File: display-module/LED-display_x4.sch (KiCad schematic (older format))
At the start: 8 parts, among them J1 Conn_DP1, J2 Conn_DP1, M1 Conn_01x01, M2 Conn_01x01, M3 Conn_01x01, M4 Conn_01x01

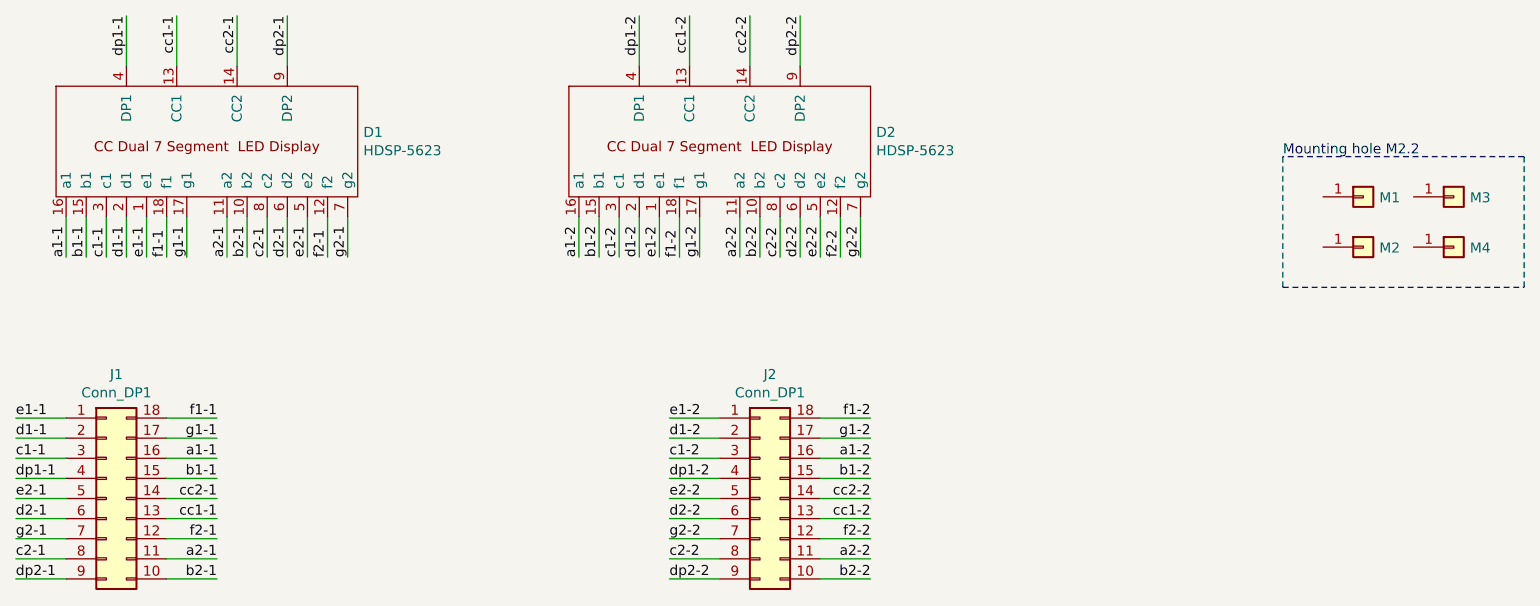
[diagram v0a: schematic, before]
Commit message: update file
I make mistake in schematics library & footprint library
now devices are correct, I divided 7 segment display at
two separate CA & CC

bye!
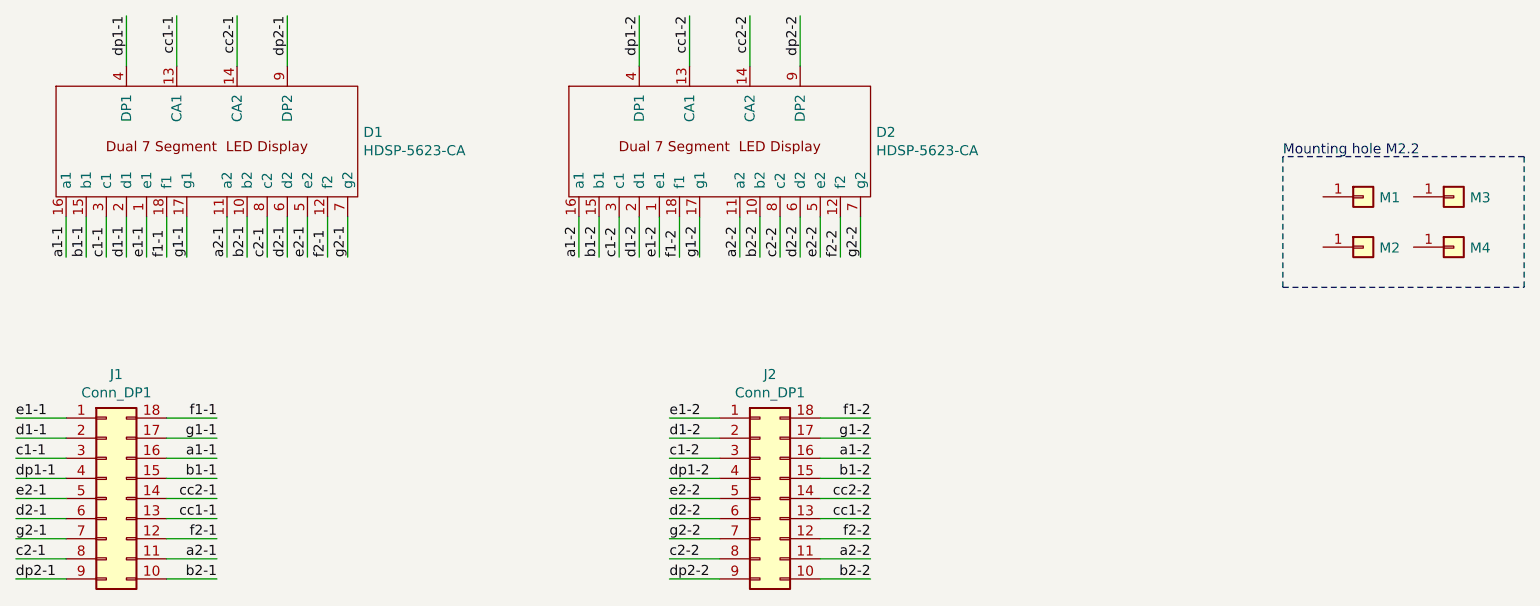
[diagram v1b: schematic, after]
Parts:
- removed D1, D2: HDSP-5623, led_display:package_led_display_0.56in_dual, symbol LED_Display:HDSP-5623
- added D1, D2: HDSP-5623-CA, led_display:package_led_display_0.56in_dual, symbol LED_Display:HDSP-5623-CA
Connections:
- net a1-1: now also D1.16 (a1)
- net a1-2: now also D2.16 (a1)
- net a2-1: now also D1.11 (a2)
- net a2-2: now also D2.11 (a2)
- net b1-1: now also D1.15 (b1)
- net b1-2: now also D2.15 (b1)
- net b2-1: now also D1.10 (b2)
- net b2-2: now also D2.10 (b2)
- net c1-1: now also D1.3 (c1)
- net c1-2: now also D2.3 (c1)
- net c2-1: now also D1.8 (c2)
- net c2-2: now also D2.8 (c2)
- net cc1-1: now also D1.13 (CA1)
- net cc1-2: now also D2.13 (CA1)
- net cc2-1: now also D1.14 (CA2)
- net cc2-2: now also D2.14 (CA2)
- net d1-1: now also D1.2 (d1)
- net d1-2: now also D2.2 (d1)
- net d2-1: now also D1.6 (d2)
- net d2-2: now also D2.6 (d2)
- net dp1-1: now also D1.4 (DP1)
- net dp1-2: now also D2.4 (DP1)
- net dp2-1: now also D1.9 (DP2)
- net dp2-2: now also D2.9 (DP2)
- net e1-1: now also D1.1 (e1)
- net e1-2: now also D2.1 (e1)
- net e2-1: now also D1.5 (e2)
- net e2-2: now also D2.5 (e2)
- net f1-1: now also D1.18 (f1)
- net f1-2: now also D2.18 (f1)
- net f2-1: now also D1.12 (f2)
- net f2-2: now also D2.12 (f2)
- net g1-1: now also D1.17 (g1)
- net g1-2: now also D2.17 (g1)
- net g2-1: now also D1.7 (g2)
- net g2-2: now also D2.7 (g2)
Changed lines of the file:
@@
 $EndDescr
-$Comp
-L LED_Display:HDSP-5623 D1
-U 1 1 5ECCCB1A
-P 3700 3400
-F 0 "D1" H 4478 3721 50  0000 L CNN
-F 1 "HDSP-5623" H 4478 3630 50  0000 L CNN
-F 2 "led_display:package_led_display_0.56in_dual" H 3150 3400 50  0001 C CNN
-F 3 "https://docs.broadcom.com/doc/AV02-1107EN" H 3150 3400 50  0001 C CNN
-	1    3700 3400
-	1    0    0    -1
-$EndComp
 $Comp
 L Connector_Generic:Conn_02x09_Counter_Clockwise J1
@@
 Text Label 3750 4700 2    50   ~ 0
 a1-1
-$Comp
-L LED_Display:HDSP-5623 D2
-U 1 1 5ECEB385
-P 6250 3400
-F 0 "D2" H 7028 3721 50  0000 L CNN
-F 1 "HDSP-5623" H 7028 3630 50  0000 L CNN
-F 2 "led_display:package_led_display_0.56in_dual" H 5700 3400 50  0001 C CNN
-F 3 "https://docs.broadcom.com/doc/AV02-1107EN" H 5700 3400 50  0001 C CNN
-	1    6250 3400
-	1    0    0    -1
-$EndComp
 Wire Wire Line
 	5550 3500 5550 3700
@@
 Text Notes 9050 3200 0    50   ~ 0
 Mounting hole M2.2
+$Comp
+L LED_Display:HDSP-5623-CA D1
+U 1 1 5EFB6DA8
+P 3700 3400
+F 0 "D1" H 4478 3721 50  0000 L CNN
+F 1 "HDSP-5623-CA" H 4478 3630 50  0000 L CNN
+F 2 "led_display:package_led_display_0.56in_dual" H 3150 3400 50  0001 C CNN
+F 3 "" H 3150 3400 50  0001 C CNN
+	1    3700 3400
+	1    0    0    -1
+$EndComp
+$Comp
+L LED_Display:HDSP-5623-CA D2
+U 1 1 5EFB75C2
+P 6250 3400
+F 0 "D2" H 7028 3721 50  0000 L CNN
+F 1 "HDSP-5623-CA" H 7028 3630 50  0000 L CNN
+F 2 "led_display:package_led_display_0.56in_dual" H 5700 3400 50  0001 C CNN
+F 3 "" H 5700 3400 50  0001 C CNN
+	1    6250 3400
+	1    0    0    -1
+$EndComp
 $EndSCHEMATC
